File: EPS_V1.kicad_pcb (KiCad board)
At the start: 2 copper layers, 82.5 x 82.5 mm, 197 parts, among them J1 Conn_01x19, J2 Conn_01x25, J3 Conn_01x9, J4 Conn_01x02, SW1 SWITCH, SW2 SWITCH, SW3 SWITCH, U1 MP2672AGD-0000-Z, U10 MP2672AGD-0000-Z, U11 MAX17205G+, U12 MP2672AGD-0000-Z, U13 MAX17205G+, U2 TPS62132RGTR, U3 TPS62133RGTR, U4 MP28167GQ-Z, U5 MAX17205G+, U6 TPS61088RHLR, U7 TPS2121RUXR, U8 MP2672AGD-0000-Z, U9 MAX17205G+

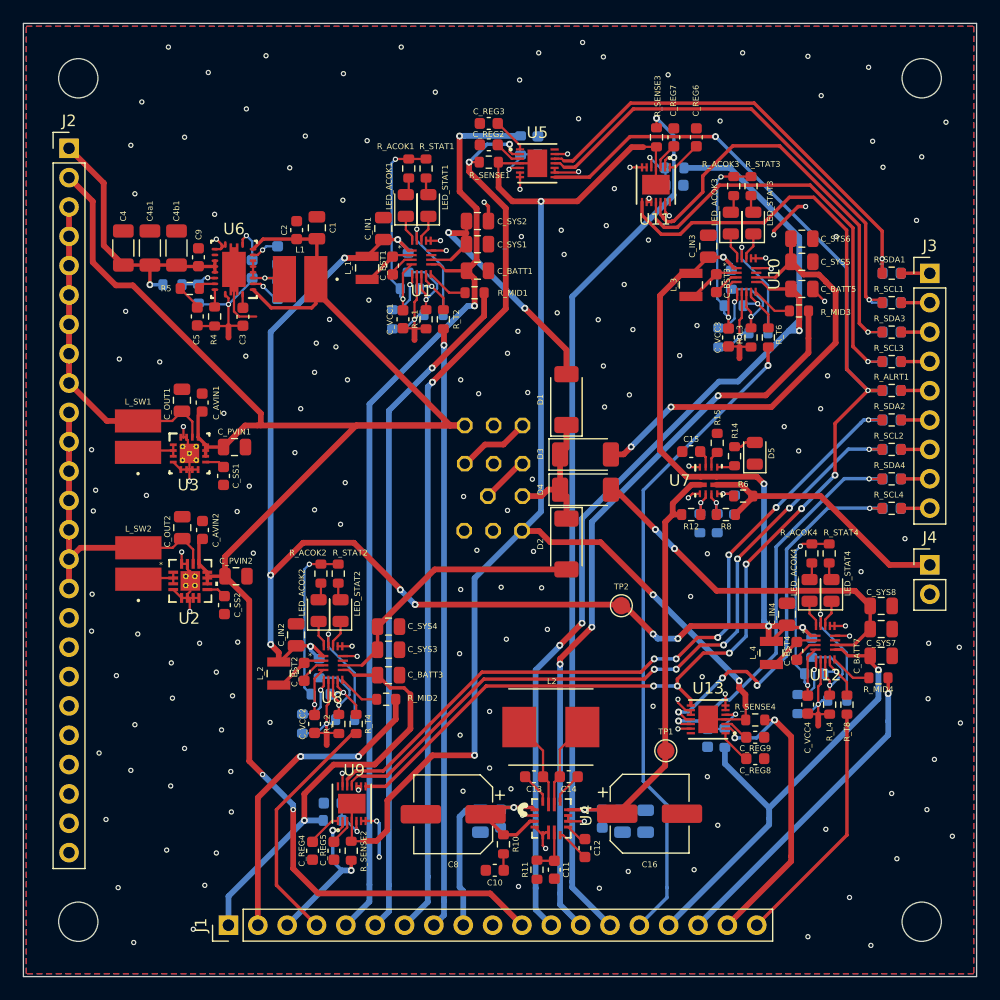
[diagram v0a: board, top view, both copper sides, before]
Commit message: Add chargers to I2C, chg_in for ADC
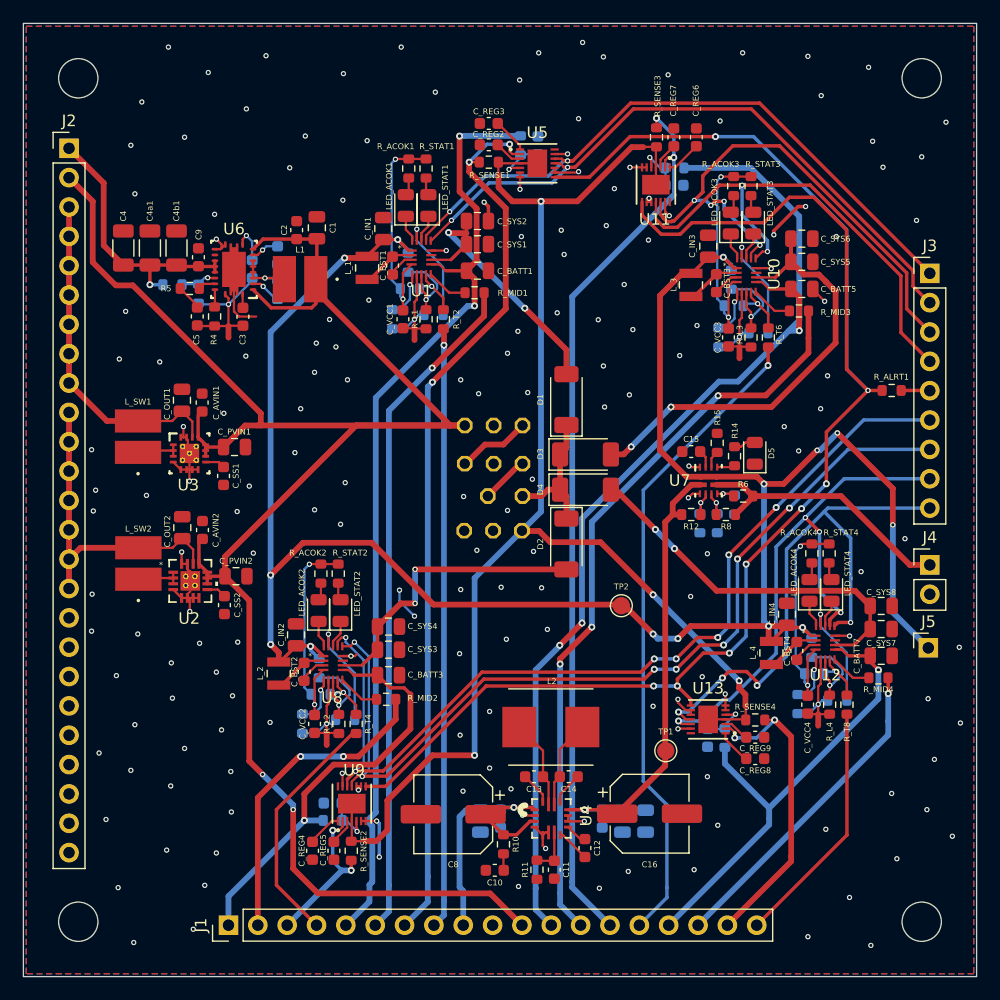
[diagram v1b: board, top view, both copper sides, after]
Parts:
- removed D_ALRT1, D_SCL1, D_SCL2, D_SCL3, D_SCL4, D_SDA1, D_SDA2, D_SDA3, D_SDA4: 4.7, Diode_SMD:D_0603_1608Metric
- removed R_SCL1, R_SCL2, R_SCL3, R_SCL4, R_SDA1, R_SDA2, R_SDA3, R_SDA4: 150R, Resistor_SMD:R_0603_1608Metric
- added J5: Conn_01x01, Connector_PinHeader_2.54mm:PinHeader_1x01_P2.54mm_Horizontal, F.Cu at (137.1, 112.8)
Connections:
- U1 pad 14: GND -> I2C1_SCL
- U1 pad 15: GND -> I2C1_SDA
- U10 pad 14: GND -> I2C3_SCL
- U10 pad 15: GND -> I2C3_SDA
- U11 pad 11: Net-(D_SCL3-K) -> I2C3_SCL
- U11 pad 12: Net-(D_SDA3-K) -> I2C3_SDA
- U12 pad 14: GND -> I2C4_SCL
- U12 pad 15: GND -> I2C4_SDA
- U13 pad 11: Net-(D_SCL4-K) -> I2C4_SCL
- U13 pad 12: Net-(D_SDA4-K) -> I2C4_SDA
- U5 pad 11: Net-(D_SCL1-K) -> I2C1_SCL
- U5 pad 12: Net-(D_SDA1-K) -> I2C1_SDA
- U8 pad 14: GND -> I2C2_SCL
- U8 pad 15: GND -> I2C2_SDA
- U9 pad 11: Net-(D_SCL2-K) -> I2C2_SCL
- U9 pad 12: Net-(D_SDA2-K) -> I2C2_SDA
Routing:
- net I2C2_SDA: track 2.48 -> 81.3 mm, vias 0 -> 7
- net I2C2_SCL: track 2.47 -> 79.6 mm, vias 0 -> 7
- net Net-(D_SDA2-K): track 64.6 -> 0.00 mm, vias 6 -> 0
- net Net-(D_SCL2-K): track 63.1 -> 0.00 mm, vias 6 -> 0
- net I2C1_SCL: track 2.47 -> 57.0 mm, vias 0 -> 2
- net I2C1_SDA: track 2.48 -> 56.3 mm, vias 0 -> 2
- net I2C4_SCL: track 2.48 -> 49.1 mm, vias 0 -> 4
- net I2C4_SDA: track 2.48 -> 48.3 mm, vias 0 -> 4
- net I2C3_SDA: track 2.48 -> 46.4 mm, vias 0 -> 4
- net Net-(D_SCL1-K): track 42.5 -> 0.00 mm, vias 1 -> 0
- net I2C3_SCL: track 2.48 -> 44.1 mm, vias 0 -> 2
- net Net-(D_SDA1-K): track 40.1 -> 0.00 mm, vias 1 -> 0
- net Net-(D_SDA3-K): track 37.0 -> 0.00 mm, vias 1 -> 0
- net Net-(D_SCL3-K): track 36.5 -> 0.00 mm, vias 1 -> 0
- net Net-(D_SDA4-K): track 34.1 -> 0.00 mm, vias 2 -> 0
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
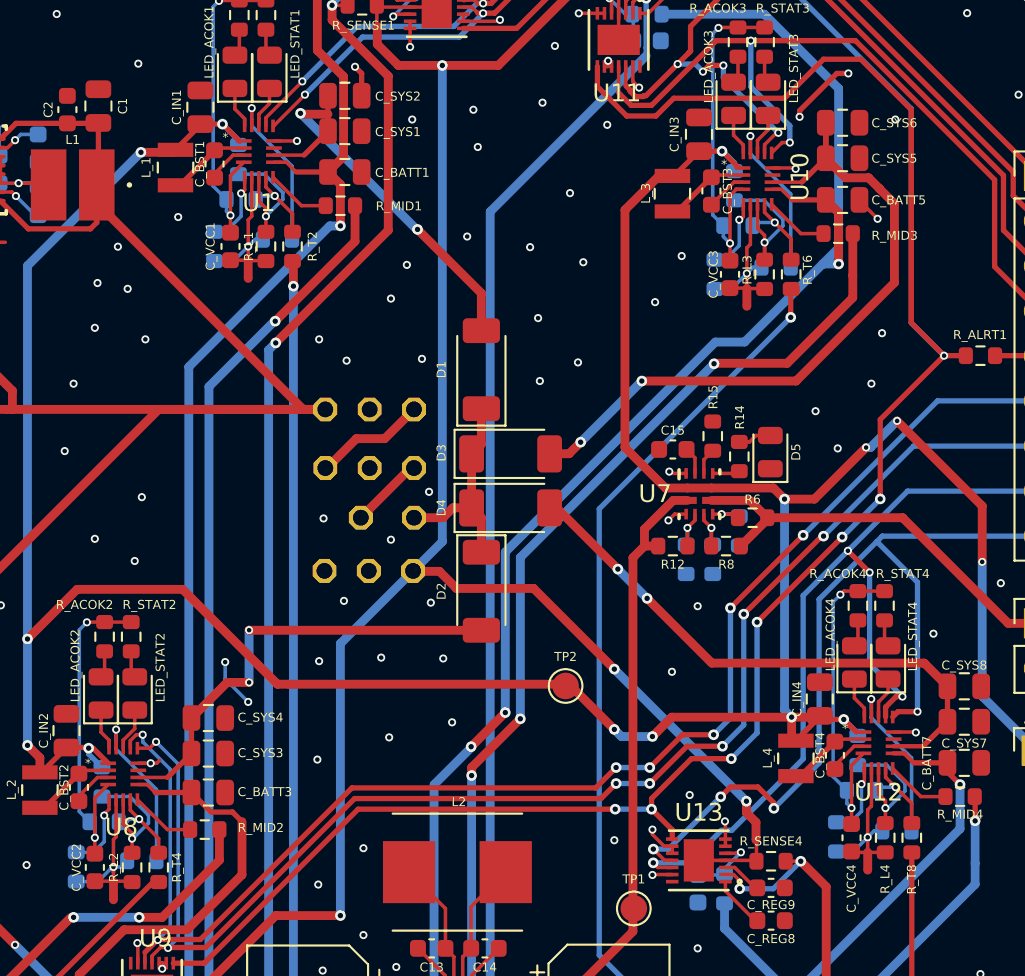
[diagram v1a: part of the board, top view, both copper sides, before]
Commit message: Fix standalone to host control mode
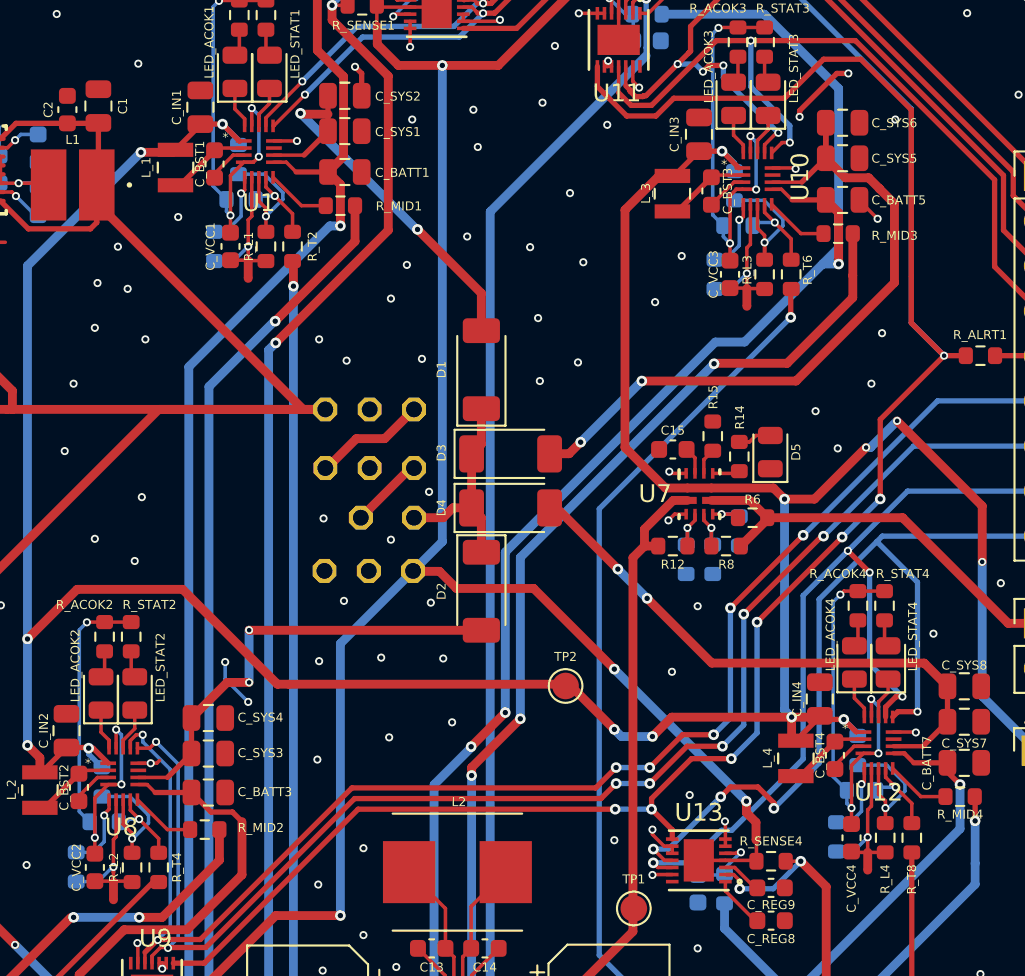
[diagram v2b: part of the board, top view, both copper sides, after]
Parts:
- removed R_VBATT1, R_VBATT2, R_VBATT3, R_VBATT4: 33k, Resistor_SMD:R_0603_1608Metric
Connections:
- C_VCC1 pad 2: Net-(U1-VCC) -> Net-(U1-CV)
- C_VCC2 pad 2: Net-(U8-VCC) -> Net-(U8-CV)
- C_VCC3 pad 2: Net-(U10-VCC) -> Net-(U10-CV)
- C_VCC4 pad 2: Net-(U12-VCC) -> Net-(U12-CV)
- R_ACOK1 pad 2: Net-(U1-VCC) -> Net-(U1-CV)
- R_ACOK2 pad 2: Net-(U8-VCC) -> Net-(U8-CV)
- R_ACOK3 pad 2: Net-(U10-VCC) -> Net-(U10-CV)
- R_ACOK4 pad 2: Net-(U12-VCC) -> Net-(U12-CV)
- R_STAT1 pad 1: Net-(U1-VCC) -> Net-(U1-CV)
- R_STAT2 pad 1: Net-(U8-VCC) -> Net-(U8-CV)
- R_STAT3 pad 1: Net-(U10-VCC) -> Net-(U10-CV)
- R_STAT4 pad 1: Net-(U12-VCC) -> Net-(U12-CV)
- R_T1 pad 1: Net-(U1-VCC) -> Net-(U1-CV)
- R_T3 pad 1: Net-(U8-VCC) -> Net-(U8-CV)
- R_T5 pad 1: Net-(U10-VCC) -> Net-(U10-CV)
- R_T7 pad 1: Net-(U12-VCC) -> Net-(U12-CV)
- U1 pad 4: Net-(U1-VCC) -> Net-(U1-CV)
- U10 pad 4: Net-(U10-VCC) -> Net-(U10-CV)
- U12 pad 4: Net-(U12-VCC) -> Net-(U12-CV)
- U8 pad 4: Net-(U8-VCC) -> Net-(U8-CV)
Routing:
- net Net-(U10-VCC): track 19.9 -> 0.00 mm, vias 2 -> 0
- net Net-(U1-VCC): track 19.7 -> 0.00 mm, vias 2 -> 0
- net Net-(U8-VCC): track 19.5 -> 0.00 mm, vias 2 -> 0
- net Net-(U12-VCC): track 19.3 -> 0.00 mm, vias 2 -> 0
- net Net-(U10-CV): track 9.29 -> 24.8 mm, vias 1 -> 4
- net Net-(U1-CV): track 9.34 -> 24.6 mm, vias 1 -> 4
- net Net-(U8-CV): track 9.39 -> 24.5 mm, vias 1 -> 4
- net Net-(U12-CV): track 9.45 -> 24.5 mm, vias 1 -> 4
- net GNDA1: track 10.1 -> 9.15 mm
- net GNDA4: track 9.81 -> 8.84 mm
- net GNDA3: track 9.94 -> 8.97 mm
- net GNDA2: track 10.2 -> 9.32 mm

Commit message: Restore EPS layout + connector changes (recovered from local snapshot)
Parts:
- added R_ADC1: 36k, Resistor_SMD:R_0603_1608Metric, B.Cu at (136.5, 118.0)
- added R_ADC2: 24k, Resistor_SMD:R_0603_1608Metric, B.Cu at (136.5, 116.0)
- R_ALRT1: value 1k -> 10k
- moved R_ALRT1 5.40 mm to (128.5, 90.5)
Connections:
- J3 pad 5: Net-(J3-Pin_5) -> ALRT
- J5 pad 1: CHG_IN -> Net-(J5-Pin_1)
- R_ALRT1 pad 1: ALRT -> +3V3
- R_ALRT1 pad 2: Net-(J3-Pin_5) -> ALRT
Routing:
- net +3V3: track 28.3 -> 143.1 mm, vias 0 -> 11
- net Net-(J5-Pin_1): track 0.00 -> 6.20 mm
- net ALRT: track 149.1 -> 155.2 mm
- net CHG_IN: track 185.7 -> 188.8 mm
- net Net-(J3-Pin_5): track 2.48 -> 0.00 mm
